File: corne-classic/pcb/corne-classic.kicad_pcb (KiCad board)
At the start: 2 copper layers, 152.8 x 92.2 mm, 100 parts, among them J1 MJ-4PP-9, J2 OLED, J3 LED, P1 i2c-pin, P2 i2c-pin, SW1 SW_PUSH, SW10 SW_PUSH, SW11 SW_PUSH, SW12 SW_PUSH, SW13 SW_PUSH, SW14 SW_PUSH, SW15 SW_PUSH, SW16 SW_PUSH, SW17 SW_PUSH, SW18 SW_PUSH, SW19 SW_PUSH, SW2 SW_PUSH, SW20 SW_PUSH, SW21 SW_PUSH, SW22 SW_PUSH, SW3 SW_PUSH, SW4 SW_PUSH, SW5 SW_PUSH, SW6 SW_PUSH, SW7 SW_PUSH, SW8 SW_PUSH, SW9 SW_PUSH, U1 ProMicro

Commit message: updated files
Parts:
- SW21: footprint kbd:MX_ALPS_PG1350_noLed -> kbd:MX_ALPS_PG1350_noLed_1.75u
- moved D22 16.0 mm to (42.9, 90.9)
- moved D13 16.0 mm to (62.0, 115.1)
- moved D7 16.0 mm to (62.0, 96.1)
- moved D1 16.0 mm to (62.0, 77.1)
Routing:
- net GND: track 0.00 -> 826.8 mm, vias 0 -> 50
- net VCC: track 0.00 -> 802.4 mm, vias 0 -> 33
- net col0: track 0.00 -> 280.4 mm, vias 0 -> 5
- net row3: track 0.00 -> 257.9 mm, vias 0 -> 6
- net col3: track 0.00 -> 229.7 mm, vias 0 -> 6
- net col1: track 0.00 -> 224.5 mm, vias 0 -> 4
- net row2: track 0.00 -> 215.8 mm, vias 0 -> 11
- net row0: track 0.00 -> 205.5 mm, vias 0 -> 3
- net col2: track 0.00 -> 200.7 mm, vias 0 -> 8
- net col4: track 0.00 -> 198.4 mm, vias 0 -> 6
- net row1: track 0.00 -> 191.7 mm, vias 0 -> 11
- net col5: track 0.00 -> 191.4 mm, vias 0 -> 2
- net LED: track 0.00 -> 77.7 mm, vias 0 -> 8
- net data: track 0.00 -> 75.1 mm, vias 0 -> 5
- net SDA: track 0.00 -> 54.9 mm, vias 0 -> 3
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
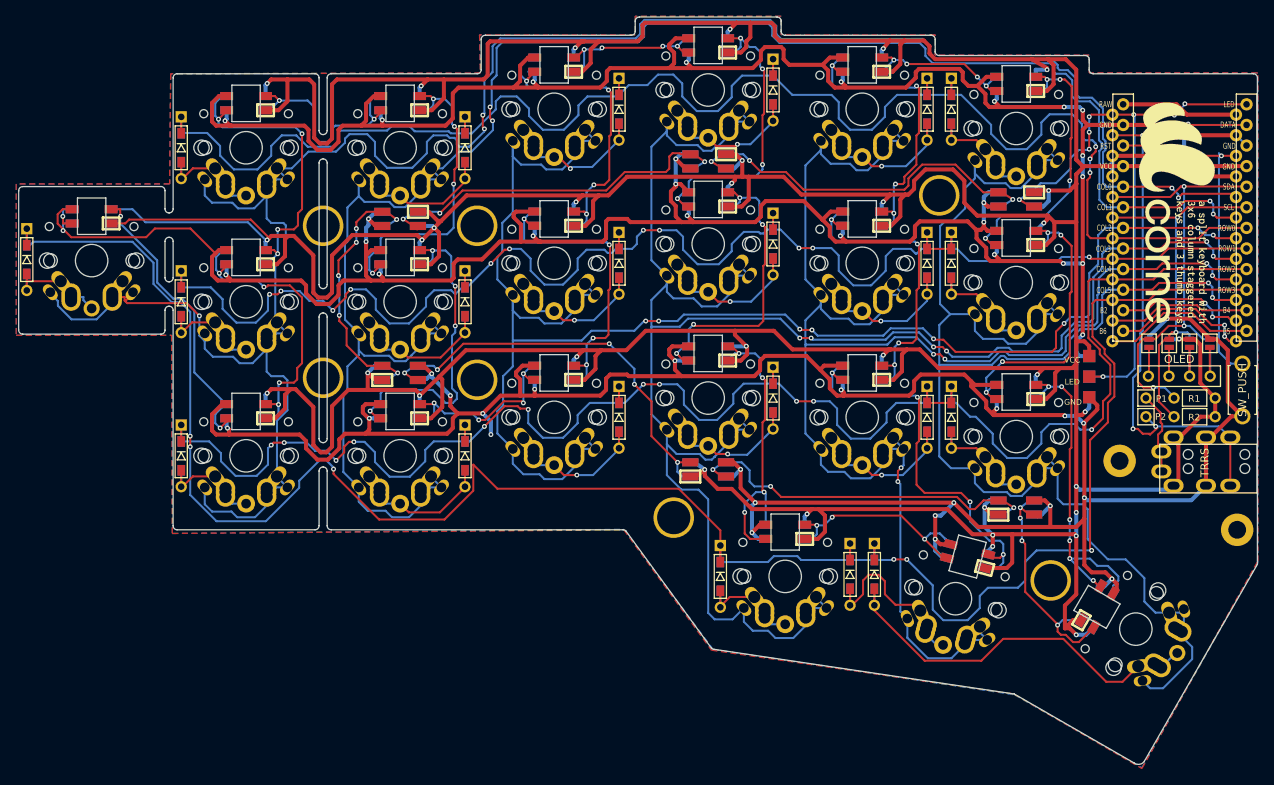
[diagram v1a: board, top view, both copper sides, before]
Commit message: added bottom plate
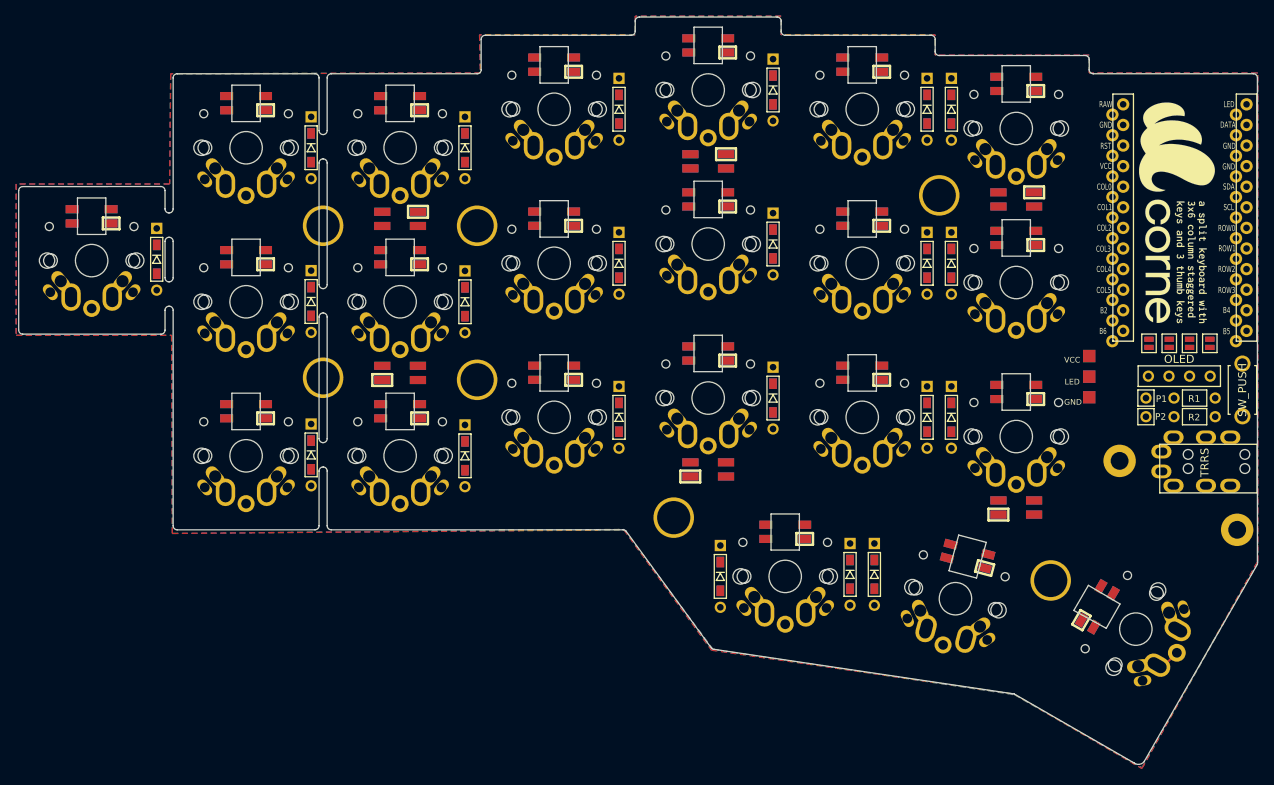
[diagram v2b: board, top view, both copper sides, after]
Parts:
- SW21: footprint kbd:MX_ALPS_PG1350_noLed_1.75u -> kbd:MX_ALPS_PG1350_noLed
- moved D22 16.0 mm to (59.0, 90.9)
- moved D13 16.0 mm to (78.0, 115.0)
- moved D7 16.0 mm to (78.0, 96.1)
- moved D1 16.0 mm to (78.0, 77.1)
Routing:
- net GND: track 826.8 -> 0.00 mm, vias 50 -> 0
- net VCC: track 802.4 -> 0.00 mm, vias 33 -> 0
- net col0: track 280.4 -> 0.00 mm, vias 5 -> 0
- net row3: track 257.9 -> 0.00 mm, vias 6 -> 0
- net col3: track 229.7 -> 0.00 mm, vias 6 -> 0
- net col1: track 224.5 -> 0.00 mm, vias 4 -> 0
- net row2: track 215.8 -> 0.00 mm, vias 11 -> 0
- net row0: track 205.5 -> 0.00 mm, vias 3 -> 0
- net col2: track 200.7 -> 0.00 mm, vias 8 -> 0
- net col4: track 198.4 -> 0.00 mm, vias 6 -> 0
- net row1: track 191.7 -> 0.00 mm, vias 11 -> 0
- net col5: track 191.4 -> 0.00 mm, vias 2 -> 0
- net LED: track 77.7 -> 0.00 mm, vias 8 -> 0
- net data: track 75.1 -> 0.00 mm, vias 5 -> 0
- net SDA: track 54.9 -> 0.00 mm, vias 3 -> 0
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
